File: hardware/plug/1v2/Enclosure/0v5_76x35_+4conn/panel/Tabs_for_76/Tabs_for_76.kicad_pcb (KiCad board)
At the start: 2 copper layers, 11.7 x 6.6 mm, 1 part, among them P1 CONN_01X01

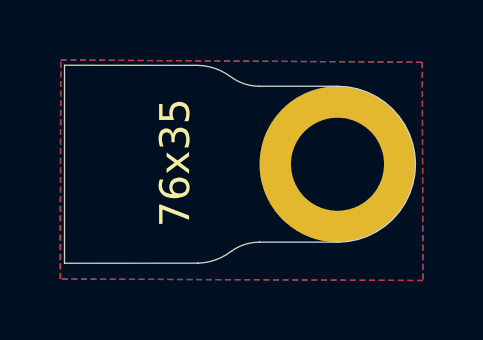
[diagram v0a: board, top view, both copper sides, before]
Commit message: 3rd batch ready for fab house
Gerber output produced
Combined into a panel

Added small holes on backside for "ventilation" #7
Naming is consistent with current LimeSDR boards W, L, H order for TX #2

Text stays on Silkscreen for now #8
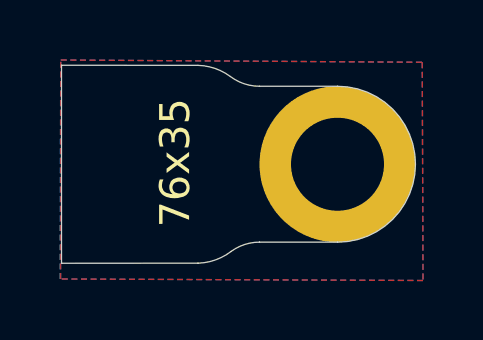
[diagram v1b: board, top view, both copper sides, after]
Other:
- board size 11.7 x 6.6 mm -> 11.8 x 6.6 mm
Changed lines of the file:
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@@
-(kicad_pcb (version 4) (host pcbnew "(2016-07-22 BZR 6991, Git 146a78a)-product")
+(kicad_pcb (version 20160815) (host pcbnew "(2016-09-17 revision 679eef1)-makepkg")
   (general
     (links 0)
     (no_connects 0)
-    (area -15.078333 -5.7275 3.360001 9.129958)
+    (area -15.078333 -5.7275 2.850001 9.145)
     (thickness 1.6)
     (drawings 3)
@@
     (pad_drill 3.3)
     (pad_to_mask_clearance 0)
-    (aux_axis_origin -9.21 -3.68)
+    (aux_axis_origin -9.26 -3.68)
+    (grid_origin -9.26 -3.68)
     (visible_elements 7FFFFFFF)
     (pcbplotparams
@@
       (drillshape 0)
       (scaleselection 1)
-      (outputdirectory Gerber/20160819_tabs/))
+      (outputdirectory ../_Gerber/20160924_tabs/))
   )
   (net 0 "")
@@
     (uvia_dia 0.3)
     (uvia_drill 0.1)
+    (diff_pair_gap 0.25)
+    (diff_pair_width 0.2)
     (add_net GND)
   )
@@
     (fp_arc (start -2.6 4.199706) (end -3.55 2.908063) (angle 36.33438316) (layer Edge.Cuts) (width 0.02))
     (fp_arc (start -4.698313 -1.403591) (end -4.652118 -3.296725) (angle 35.17359225) (layer Edge.Cuts) (width 0.02))
-    (fp_line (start -9.1 3.3) (end -4.651552 3.297548) (layer Edge.Cuts) (width 0.02))
-    (fp_line (start -9.1 -3.3) (end -9.1 3.3) (layer Edge.Cuts) (width 0.02))
-    (fp_line (start -4.652118 -3.296725) (end -9.1 -3.3) (layer Edge.Cuts) (width 0.02))
+    (fp_line (start -9.2 3.3) (end -4.651552 3.297548) (layer Edge.Cuts) (width 0.02))
+    (fp_line (start -9.2 -3.3) (end -9.2 3.3) (layer Edge.Cuts) (width 0.02))
+    (fp_line (start -4.652118 -3.296725) (end -9.2 -3.3) (layer Edge.Cuts) (width 0.02))
     (fp_line (start -2.6 2.596322) (end 0 2.596322) (layer Edge.Cuts) (width 0.02))
     (fp_line (start 0 -2.6) (end -2.6 -2.6) (layer Edge.Cuts) (width 0.02))
@@
     (effects (font (size 1 1) (thickness 0.1)))
   )
-  (dimension 9.100049 (width 0.3) (layer Dwgs.User)
-    (gr_text "9.100 mm" (at -4.575549 7.734957 -0.1888865009) (layer Dwgs.User)
+  (dimension 9.2 (width 0.3) (layer Dwgs.User)
+    (gr_text "9.200 mm" (at -4.6 7.749999) (layer Dwgs.User)
       (effects (font (size 1.5 1.5) (thickness 0.3)))
     )
-    (feature1 (pts (xy -9.1 -0.03) (xy -9.13 9.06995)))
-    (feature2 (pts (xy 0 0) (xy -0.03 9.09995)))
-    (crossbar (pts (xy -0.021099 6.399965) (xy -9.121099 6.369965)))
-    (arrow1a (pts (xy -9.121099 6.369965) (xy -7.992668 5.787261)))
-    (arrow1b (pts (xy -9.121099 6.369965) (xy -7.996535 6.960096)))
-    (arrow2a (pts (xy -0.021099 6.399965) (xy -1.145663 5.809834)))
-    (arrow2b (pts (xy -0.021099 6.399965) (xy -1.14953 6.982669)))
+    (feature1 (pts (xy -9.2 0) (xy -9.2 9.099999)))
+    (feature2 (pts (xy 0 0) (xy 0 9.099999)))
+    (crossbar (pts (xy 0 6.399999) (xy -9.2 6.399999)))
+    (arrow1a (pts (xy -9.2 6.399999) (xy -8.073496 5.813578)))
+    (arrow1b (pts (xy -9.2 6.399999) (xy -8.073496 6.98642)))
+    (arrow2a (pts (xy 0 6.399999) (xy -1.126504 5.813578)))
+    (arrow2b (pts (xy 0 6.399999) (xy -1.126504 6.98642)))
   )
   (zone (net 0) (net_name "") (layer B.Mask) (hatch edge 0.508)
@@
     (polygon
       (pts
-        (xy -9.083005 3.67) (xy -6.923005 3.67) (xy -6.943005 -3.59) (xy -9.103005 -3.59)
+        (xy -9.183005 3.67) (xy -7.023005 3.67) (xy -7.043005 -3.59) (xy -9.203005 -3.59)
       )
     )
@@
     (polygon
       (pts
-        (xy -9.083409 3.666033) (xy -6.923409 3.666033) (xy -6.943409 -3.593967) (xy -9.103409 -3.593967)
+        (xy -9.183409 3.666033) (xy -7.023409 3.666033) (xy -7.043409 -3.593967) (xy -9.203409 -3.593967)
       )
     )
